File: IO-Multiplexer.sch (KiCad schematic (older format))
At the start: 15 parts

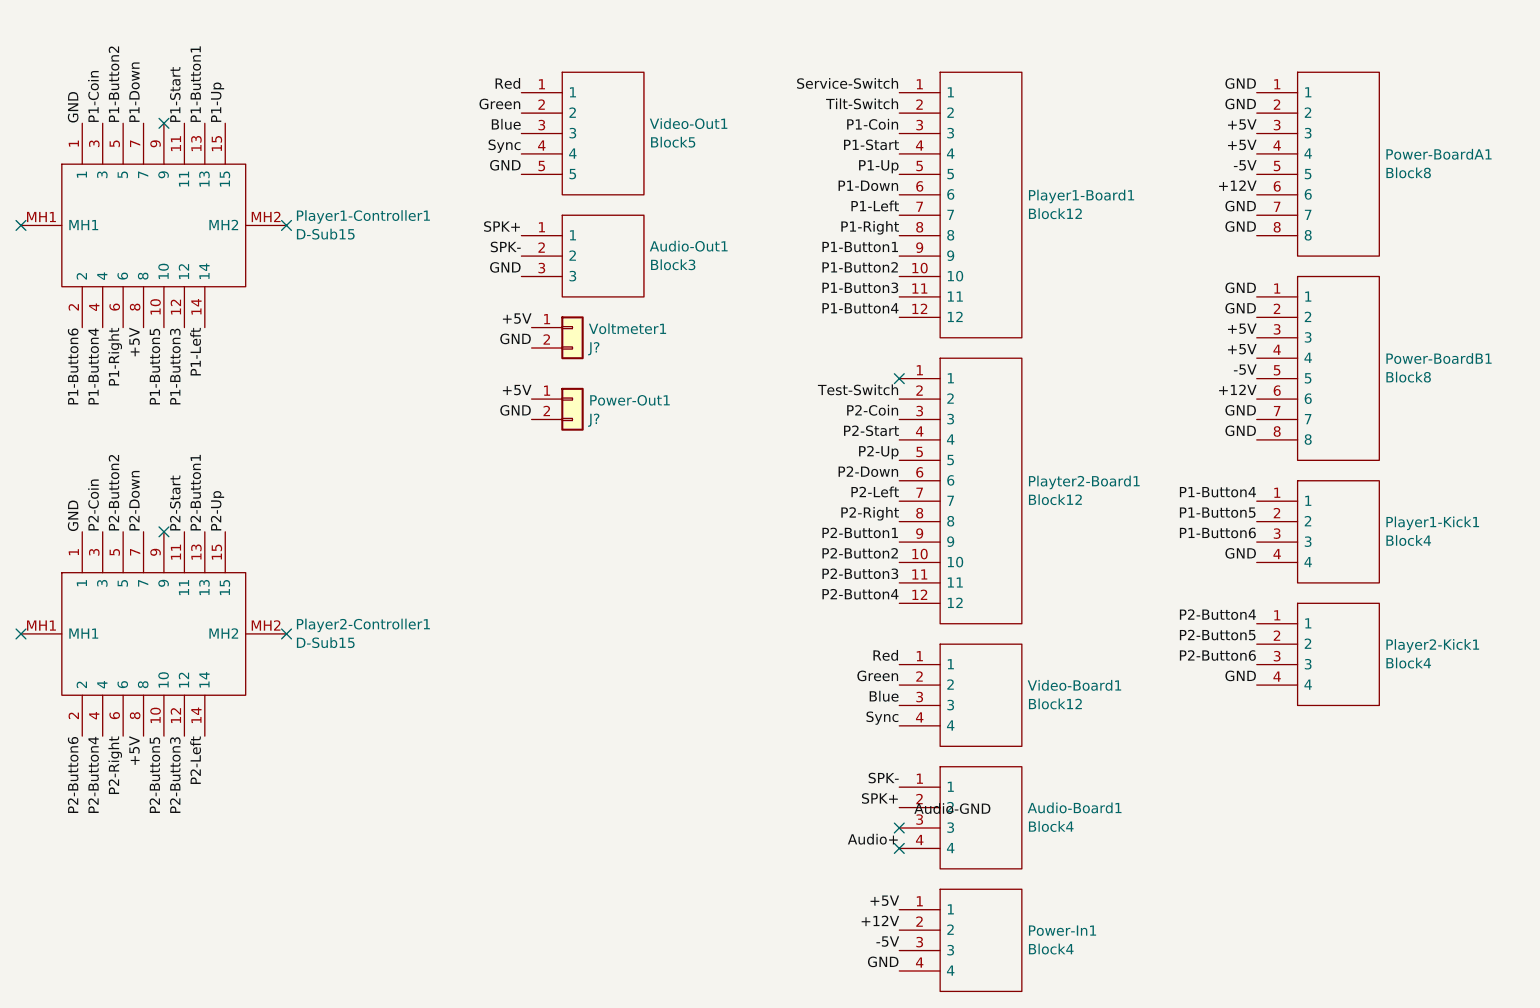
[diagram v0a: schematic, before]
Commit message: Update to neo-geo plus pinout
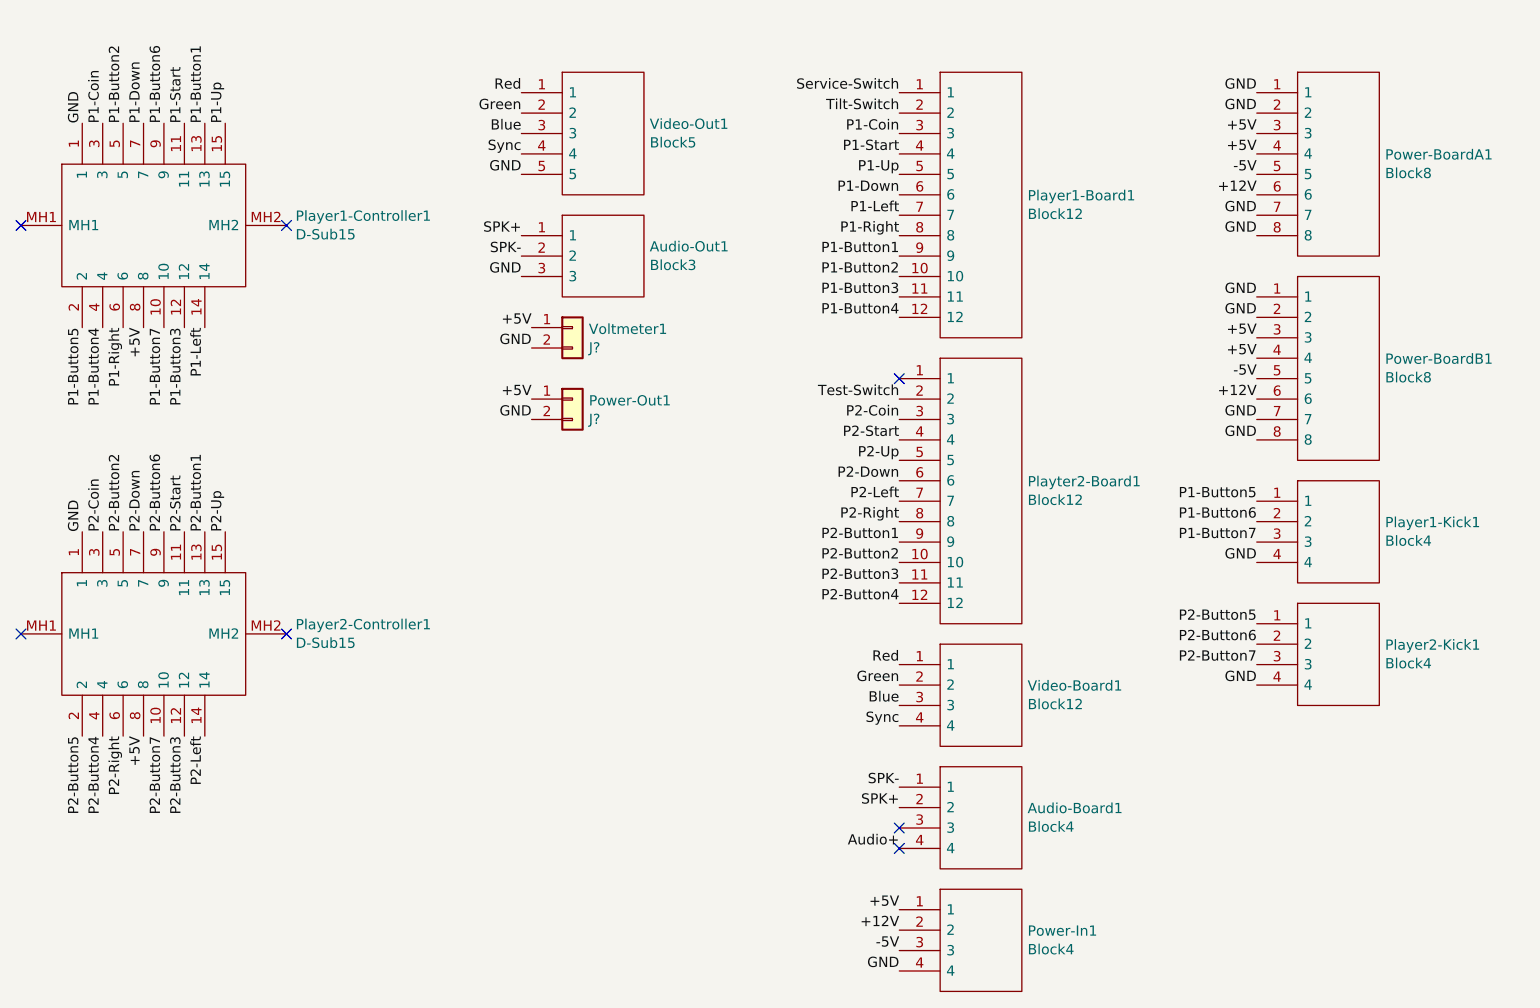
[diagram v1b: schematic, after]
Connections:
- net P1-Button4: no longer Player1-Kick1.1
- net P1-Button5: now also Player1-Controller1.2, Player1-Kick1.1; no longer Player1-Controller1.10, Player1-Kick1.2
- net P1-Button6: now also Player1-Controller1.9, Player1-Kick1.2; no longer Player1-Controller1.2, Player1-Kick1.3
- net P2-Button4: no longer Player2-Kick1.1
- net P2-Button5: now also Player2-Controller1.2, Player2-Kick1.1; no longer Player2-Controller1.10, Player2-Kick1.2
- net P2-Button6: now also Player2-Controller1.9, Player2-Kick1.2; no longer Player2-Controller1.2, Player2-Kick1.3
- new net P1-Button7: Player1-Controller1.10, Player1-Kick1.3
- new net P2-Button7: Player2-Controller1.10, Player2-Kick1.3
- no-connect marks 9 -> 7
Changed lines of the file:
@@
-$EndComp
-$Comp
-L SamacSys_Parts:TB001-500-04BE Audio-Board1
-U 1 1 5EEF5EBA
-P 7150 4350
-F 0 "Audio-Board1" H 7778 4246 50  0000 L CNN
-F 1 "Block4" H 7778 4155 50  0000 L CNN
-F 2 "SamacSys:TB00150004BE" H 7800 4450 50  0001 L CNN
-F 3 "https://componentsearchengine.com/Datasheets/1/TB001-500-04BE.pdf" H 7800 4350 50  0001 L CNN
-F 4 "Fixed Terminal Blocks Terminal block, screw type, 5.00, horizontal, 4 poles, CUI Blue, slotted screw, PCB mount" H 7800 4250 50  0001 L CNN "Description"
-F 5 "12.9" H 7800 4150 50  0001 L CNN "Height"
-F 6 "490-TB001-500-04BE" H 7800 4050 50  0001 L CNN "Mouser Part Number"
-F 7 "https://www.mouser.co.uk/ProductDetail/CUI-Devices/TB001-500-04BE?qs=vLWxofP3U2xFd1xqNcHXZA%3D%3D" H 7800 3950 50  0001 L CNN "Mouser Price/Stock"
-F 8 "CUI Devices" H 7800 3850 50  0001 L CNN "Manufacturer_Name"
-F 9 "TB001-500-04BE" H 7800 3750 50  0001 L CNN "Manufacturer_Part_Number"
-	1    7150 4350
-	1    0    0    -1
 $EndComp
 $Comp
@@
 Text Label 7150 4050 2    50   ~ 0
 Sync
-Text Label 7150 4450 2    50   ~ 0
-SPK+
 Text Label 7150 4350 2    50   ~ 0
 SPK-
-Text Label 7600 4500 2    50   ~ 0
-Audio-GND
 Text Label 7150 4650 2    50   ~ 0
 Audio+
@@
 P1-Up
 Text Label 3150 2100 3    50   ~ 0
-P1-Button6
+P1-Button5
 Text Label 3250 2100 3    50   ~ 0
 P1-Button4
@@
 +5V
 Text Label 3550 2100 3    50   ~ 0
-P1-Button5
+P1-Button7
 Text Label 3650 2100 3    50   ~ 0
 P1-Button3
@@
 P2-Up
 Text Label 3150 4100 3    50   ~ 0
-P2-Button6
+P2-Button5
 Text Label 3250 4100 3    50   ~ 0
 P2-Button4
@@
 +5V
 Text Label 3550 4100 3    50   ~ 0
-P2-Button5
+P2-Button7
 Text Label 3650 4100 3    50   ~ 0
 P2-Button3
 Text Label 3750 4100 3    50   ~ 0
 P2-Left
-Text Label 7150 950  2    50   ~ 0
-Service-Switch
-Text Label 7150 1050 2    50   ~ 0
-Tilt-Switch
 Text Label 7150 1150 2    50   ~ 0
 P1-Coin
@@
 Text Label 7150 2650 2    50   ~ 0
 P2-Start
-NoConn ~ 7150 4550
 NoConn ~ 7150 4650
 $Comp
@@
 $EndComp
 Text Label 8900 2950 2    50   ~ 0
-P1-Button4
+P1-Button5
 Text Label 8900 3050 2    50   ~ 0
-P1-Button5
+P1-Button6
 Text Label 8900 3150 2    50   ~ 0
-P1-Button6
+P1-Button7
 Text Label 8900 3250 2    50   ~ 0
 GND
@@
 $EndComp
 Text Label 8900 3550 2    50   ~ 0
-P2-Button4
+P2-Button5
 Text Label 8900 3650 2    50   ~ 0
-P2-Button5
+P2-Button6
 Text Label 8900 3750 2    50   ~ 0
-P2-Button6
+P2-Button7
 Text Label 8900 3850 2    50   ~ 0
 GND
@@
 $EndComp
 NoConn ~ 7150 2350
+NoConn ~ 7150 4550
+Text Label 7150 4450 2    50   ~ 0
+SPK+
+$Comp
+L SamacSys_Parts:TB001-500-04BE Audio-Board1
+U 1 1 5EEF5EBA
+P 7150 4350
+F 0 "Audio-Board1" H 7778 4246 50  0000 L CNN
+F 1 "Block4" H 7778 4155 50  0000 L CNN
+F 2 "SamacSys:TB00150004BE" H 7800 4450 50  0001 L CNN
+F 3 "https://componentsearchengine.com/Datasheets/1/TB001-500-04BE.pdf" H 7800 4350 50  0001 L CNN
+F 4 "Fixed Terminal Blocks Terminal block, screw type, 5.00, horizontal, 4 poles, CUI Blue, slotted screw, PCB mount" H 7800 4250 50  0001 L CNN "Description"
+F 5 "12.9" H 7800 4150 50  0001 L CNN "Height"
+F 6 "490-TB001-500-04BE" H 7800 4050 50  0001 L CNN "Mouser Part Number"
+F 7 "https://www.mouser.co.uk/ProductDetail/CUI-Devices/TB001-500-04BE?qs=vLWxofP3U2xFd1xqNcHXZA%3D%3D" H 7800 3950 50  0001 L CNN "Mouser Price/Stock"
+F 8 "CUI Devices" H 7800 3850 50  0001 L CNN "Manufacturer_Name"
+F 9 "TB001-500-04BE" H 7800 3750 50  0001 L CNN "Manufacturer_Part_Number"
+	1    7150 4350
+	1    0    0    -1
+$EndComp
 Text Label 7150 2450 2    50   ~ 0
 Test-Switch
-NoConn ~ 3550 3100
-NoConn ~ 3550 1100
+Text Label 7150 1050 2    50   ~ 0
+Tilt-Switch
+Text Label 7150 950  2    50   ~ 0
+Service-Switch
+Text Label 3550 1100 1    50   ~ 0
+P1-Button6
+Text Label 3550 3100 1    50   ~ 0
+P2-Button6
 $EndSCHEMATC
